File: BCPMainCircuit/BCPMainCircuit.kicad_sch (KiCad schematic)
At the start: 48 parts, among them Q1 IRLB8721PBF, SW1 Switch, U1 MCP9601T-E/MX, U2 Pico 2, U3 Logger, U4 GPS, U5 BNO055, U6 BME280, U7 MIC2940A-3.3WT, U8 MCP9601T-E/MX

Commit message: minor changes n stuff
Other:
- note added: "https://www.sparkfun.com/sparkfun-multiplexer-breakout-8-channel-74hc4051.html"
- moved on the sheet: C3, C4, R10, R11, R12, R13, R14, R15, R16, R17, R18, R5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

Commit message: e
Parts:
- added C10: 4u7F, Capacitor_SMD:C_0603_1608Metric, symbol Device:C_Small
- added C11, C5: 1uF, Capacitor_SMD:C_0603_1608Metric, symbol Device:C_Small
- added C6: 10uF, Capacitor_SMD:C_0805_2012Metric, symbol Device:C_Small
- added C7: 100nF, Capacitor_SMD:C_0603_1608Metric, symbol Device:C_Small
- added C8, C9: 22uF, Capacitor_SMD:C_0805_2012Metric, symbol Device:C_Small
- added J1: MSD-4-A, CUI_MSD-4-A:CUI_MSD-4-A, symbol Cosmos Schematic Symbols:MSD-4-A
- added L1: 4u7H, 74438357047:74438357047, symbol Device:L
- added RN1, RN2: CAY16-4702F4LF, CAY16-4702F4LF:RESCAF80P320X160X60-8N, symbol Cosmos Schematic Symbols:CAY16-4702F4LF
- added U9: AP63203WU-7, AP63203WU-7_DIO:AP63203WU-7_DIO, symbol Cosmos Schematic Symbols:AP63203WU-7
- R1: value ???R -> 20Ω
- R2, R3: value ???R -> 65Ω
- R4: value ???R -> 65v
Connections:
- net GND: now also C10.2, C11.2, C5.2, C6.2, C8.2, C9.2, J1.6 (VSS), J1.G1 (COVER_GND), J1.G2 (COVER_GND__1), J1.G3 (COVER_GND__2), J1.G4 (COVER_GND__3), U9.4 (GND)
- new net: C7.2, L1.2, U9.5 (SW)
- new net: C7.1, U9.6 (BST)
- new net: J1.1 (DAT2), RN2.8
- new net: J1.8 (DAT1), RN1.5
- new net +3V3: C10.1, C11.1, C5.1, C8.1, C9.1, J1.4 (VDD), L1.1, RN1.1, RN1.2, RN1.3, RN1.4, RN2.1, RN2.2, RN2.3, RN2.4, U9.1 (FB)
- new net BATT+: C6.1, U9.2 (EN), U9.3 (VIN)
- new net SD_CD: J1.CD, RN2.6
- new net SD_CS: J1.2 (CD/DAT3), RN2.7
- new net SD_MISO: J1.7 (DAT0), RN1.7
- new net SD_MOSI: J1.3 (CMD), RN1.6
- new net SD_SCK: J1.5 (CLK), RN1.8
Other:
- note added: "47k resistor network"
- note added: "Thermocouple Amplifier"
- note added: "Thermocouples + Multiplexers"
- note added: "microSD card connector"
- note added: "sd cd = card detect"
- note removed: "Thermals"
- moved on the sheet: C3, C4, R10, R11, R12, R13, R14, R15, R16, R17, R18, R5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

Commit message: e
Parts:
- R4: value 65v -> 65Ω
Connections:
- net +3.3V: now also C10.1, C11.1, C8.1, C9.1, L1.1, U9.1 (FB)
- net +3V3: no longer C10.1, C11.1, C8.1, C9.1, L1.1, U9.1 (FB)
- net BATT+: now also SW1.3 (A)
- net SD_CD: now also U2.27 (GPIO21)
- net SD_CS: now also U2.22 (GPIO17)
- net SD_MISO: now also U2.21 (GPIO16)
- net SD_MOSI: now also U2.25 (GPIO19)
- net SD_SCK: now also U2.24 (GPIO18)
- net TC-Sel1: now also U2.15 (GPIO11); no longer U2.27 (GPIO21)
- net TC-Sel2: now also U2.16 (GPIO12); no longer U2.26 (GPIO20)
- net TC-Sel3: now also U2.17 (GPIO13); no longer U2.25 (GPIO19)
- net ThermoOCwarn: now also U2.19 (GPIO14); no longer U2.22 (GPIO17)
- net ThermoSCwarn: now also U2.20 (GPIO15); no longer U2.21 (GPIO16)
- net at C1.1, U7.1 (IN): no longer SW1.3 (A)
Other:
- moved on the sheet: C1, C10, C11, C2, C5, C6, C7, C8, C9, J1, L1, R5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

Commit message: minor stuff working on SD card thing and tc amp and power Next steps: SMD components!!!
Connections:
- net +3.3V: now also J1.4 (VDD)
- net +3V3: no longer J1.4 (VDD)
- net VSense1: now also C3.1, R10.2, U1.2 (VIN+)
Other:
- note added: "TRASH?"
- moved on the sheet: C1, C2, C4, C5, J1, R12, R13, R14, R15, R16, R17, R18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

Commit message: lsm6dso
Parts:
- removed U5: BNO055, Trantor:BNO055, symbol Trantor:BNO055
- added C12, C13: 0u1f, symbol Device:C_Small
- added R19, R20: 10kΩ, Resistor_THT:R_Axial_DIN0207_L6.3mm_D2.5mm_P7.62mm_Horizontal, symbol Device:R_Small_US
- added U10: LSM6DSO, LGA-14L_2P5X3X0P86_STM, symbol LSM6DSO:LSM6DSO
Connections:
- net +3.3V: now also C12.1, C13.1, R19.1, R20.2, U10.5 (VDDIO), U10.8 (VDD)
- net GND: now also C12.2, C13.2, U10.2 (SDx), U10.3 (SCx), U10.6 (GND), U10.7 (GND)
- net SCL: now also R20.1, U10.13 (SCL)
- net SDA: now also R19.2, U10.14 (SDA)
- no-connect marks 30 -> 29
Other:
- note added: "ADDR:"
- note added: "SMD components make the jst connector 1x4 instead of 2 1x2s Breakout pins consider 16:2 SMD Mux"
- note removed: "ADDR: 29/28"
- note removed: "NOTES Flight LED moved to GPIO22 Debug LEDs moved to GPIO 7,8,9 IN REVERSE ORDER! ThermoSelect pins are 19,20,21 IN REVERSE ORDER! note: to use, just set the pins you need high, i can explain later"

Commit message: minor changes (everything is being redone using smd components instead of breakout boards) still need : gps antenna + schematic (capacitors?) IMU (current one needs 1.8v!!!!!!!!!!!!!!!!) RGB LEDs? 16:2 mux? sd card needs reviewing (why are things laid out that way???)
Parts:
- removed C1, C2: 10u, Capacitor_THT:C_Disc_D7.0mm_W2.5mm_P5.00mm, symbol Device:C
- removed C4: 0u1f, Capacitor_SMD:C_0201_0603Metric, symbol Device:C_Small
- removed R12, R16: 2M, Resistor_SMD:R_0201_0603Metric, symbol Device:R_US
- removed R13, R14: 100, Resistor_SMD:R_0201_0603Metric, symbol Device:R_US
- removed R15: 1M, Resistor_SMD:R_0201_0603Metric, symbol Device:R_US
- removed R17, R18: 10k, Resistor_SMD:R_0201_0603Metric, symbol Device:R_US
- removed U3: Logger, Trantor:MODULE_DEV-13712, symbol Trantor:DEV-13712
- removed U4: GPS, Gabriel_footprints:NEO-M9N GPS, symbol Trantor:GPS
- removed U6: BME280, Gabriel_footprints:BMP280, symbol Trantor:BME280
- removed U7: MIC2940A-3.3WT, Package_TO_SOT_THT:TO-220-3_Vertical, symbol Regulator_Linear:L7805
- removed U8: MCP9601T-E/MX, MQFN20_NU_MCH, symbol SMD_TC_AMP:MCP9601T-E_MX
- added C1: 200nf, Capacitor_SMD:C_0201_0603Metric, symbol Device:C_Small
- added R12, R13: 4.7kΩ, Resistor_SMD:R_0201_0603Metric, symbol Device:R_Small_US
- added U3: NEO-M9N-00B, Gabriel_footprints:NEO-M9N, symbol NEO-M9N:NEO-M9N-00B
- added U4: ICM-20948, Sensor_Motion:InvenSense_QFN-24_3x3mm_P0.4mm, symbol Sensor_Motion:ICM-20948
- added U5: BME280, Gabriel_footprints:BME280(1), symbol Sensor:BME280
- BT2: footprint Battery:BatteryHolder_Keystone_2462_2xAA -> Gabriel_footprints:BAT_1079
- C12, C13: footprint (none) -> Capacitor_SMD:C_0201_0603Metric
- J1: footprint CUI_MSD-4-A:CUI_MSD-4-A -> Gabriel_footprints:CUI_MSD-4-A
- L1: footprint 74438357047:74438357047 -> Inductor_SMD:L_0201_0603Metric
- R19, R20: footprint Resistor_THT:R_Axial_DIN0207_L6.3mm_D2.5mm_P7.62mm_Horizontal -> Resistor_SMD:R_0201_0603Metric
- RN1, RN2: footprint CAY16-4702F4LF:RESCAF80P320X160X60-8N -> Resistor_SMD:R_Array_Convex_4x1206
- TC2: footprint Connector_PinHeader_2.54mm:PinHeader_1x02_P2.54mm_Vertical -> (none)
- U1: footprint MQFN20_NU_MCH -> Gabriel_footprints:MQFN20_NU_MCH
- U10: footprint LGA-14L_2P5X3X0P86_STM -> (none)
- U9: footprint AP63203WU-7_DIO:AP63203WU-7_DIO -> Package_TO_SOT_SMD:TSOT-23-6
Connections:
- net +3V3 is gone; now on net +3.3V: C5.1, RN1.1, RN1.2, RN1.3, RN1.4, RN2.1, RN2.2, RN2.3, RN2.4
- net +3.3V: now also C1.1, R12.1, R13.2, U3.2 (D_SEL), U3.23 (VCC), U5.2 (CSB), U5.5 (SDO), U5.6 (VDDIO), U5.8 (VDD)
- net GND: now also C1.2, U3.10 (GND), U3.12 (GND), U3.13 (GND), U3.24 (GND), U5.1 (GND), U5.7 (GND)
- net SCL: now also R12.2, U3.19 (SCL_/_SPI_SLK), U5.4 (SCK)
- net SDA: now also R13.1, U3.18 (SDA_/_SPI_CS_N), U5.3 (SDI)
- net TimePulseGPS: now reaches U2.4 (GPIO2)
- net TimePulseGPS: now also U3.3 (TIMEPULSE)
- new net: U4.18 (GND), U4.20 (GND)
- new net +1.8V: U4.8 (VDDIO)
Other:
- note added: "Check Capacitor/Resistor sizes!!!!!!!!"
- note added: "gps antenna?????? Backup battery for faster start??? btw timepulse is a good error indicator capacitors????"
- note added: "https://www.sdcard.org/downloads/pls/pdf/?p=Part1_Physical_Layer_Simplified_Specification_Ver9.10.jpg&f=Part1PhysicalLayerSimplifiedSpecificationVer9.10Fin_20231201.pdf&e=EN_SS9_1"
- note added: "wtf is happening??"
- note removed: "60"
- note removed: "61"
- note removed: "62"
- note removed: "63"
- note removed: "64"
- note removed: "65"
- note removed: "66"
- note removed: "67"
- note removed: "TRASH?"
- moved on the sheet: C12, C13, R19, R20, U10

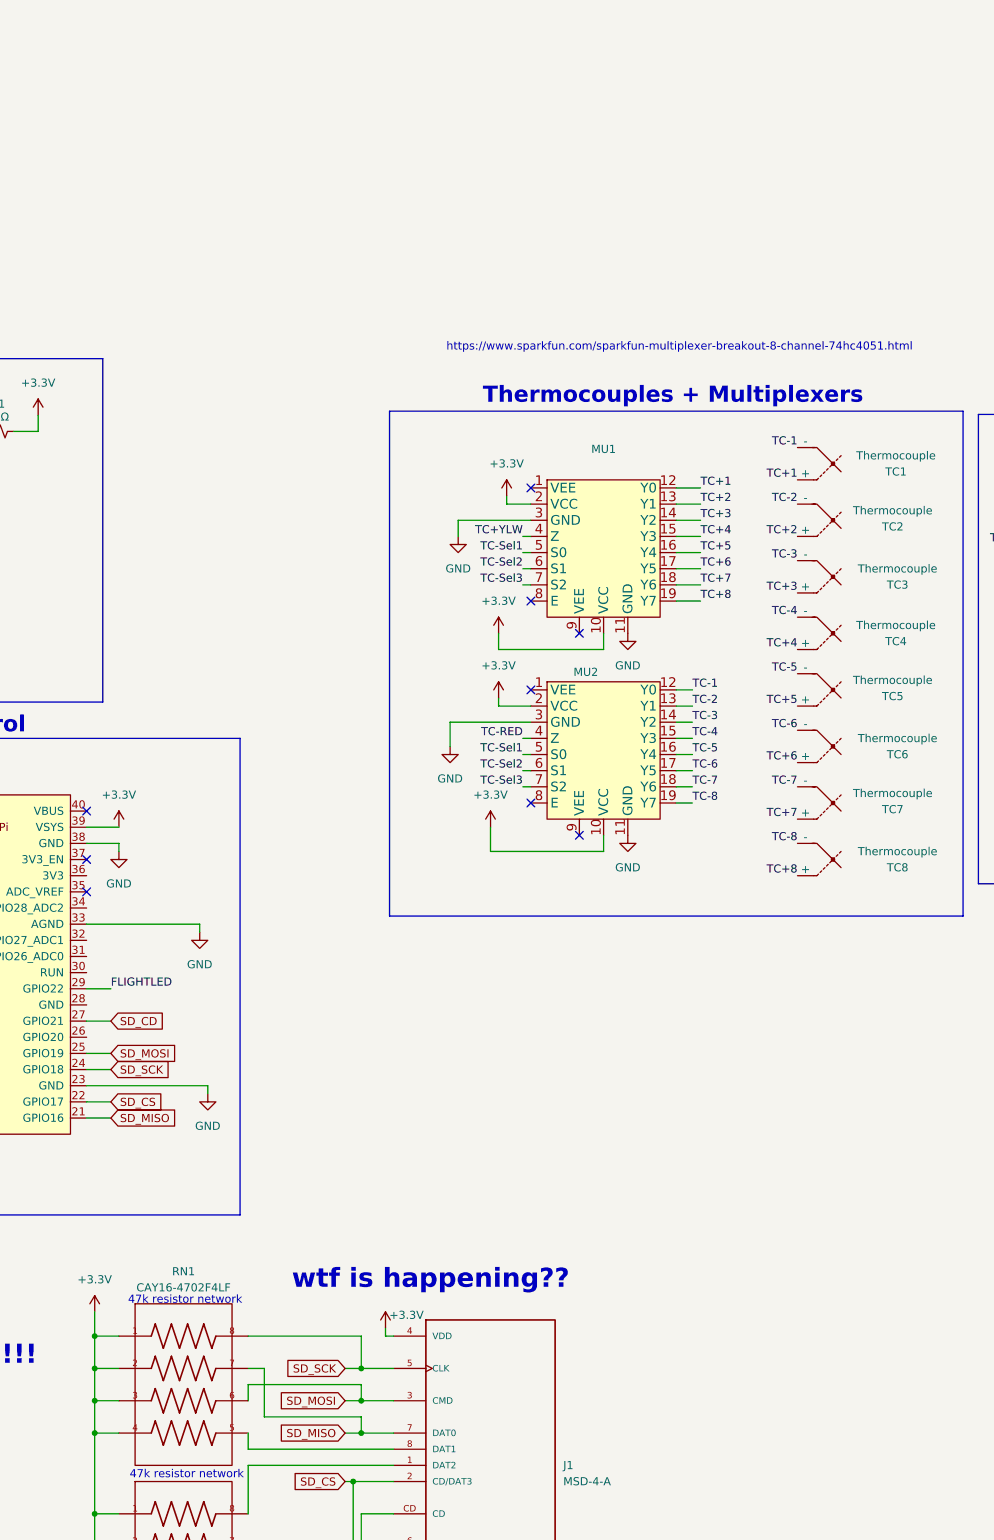
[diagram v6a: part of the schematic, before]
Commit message: in the middle of stuff NOTES: replace 2xmux with 1x cheaper mux? RGB leds HOW? how to sd card? magnetometer trade check stock of resistors, capacitors, inductors, sd slots, etc etc
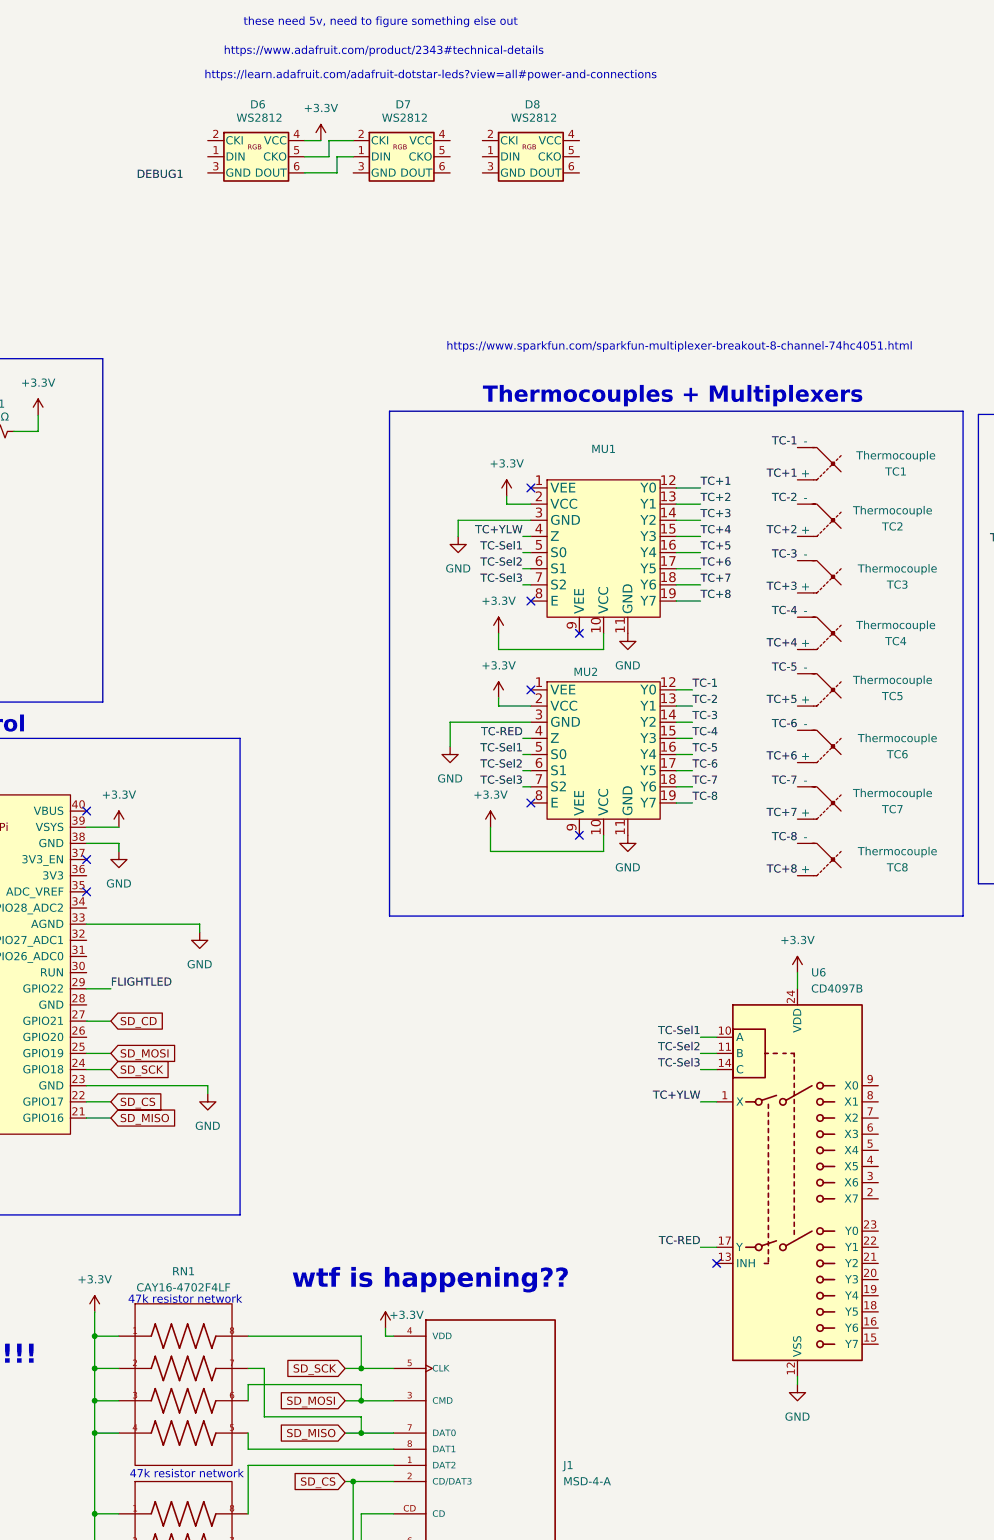
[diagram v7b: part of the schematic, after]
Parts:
- added D6, D7, D8: WS2812, LED_SMD:LED_WS2812_PLCC6_5.0x5.0mm_P1.6mm, symbol LED:WS2812
- added U6: CD4097B, symbol Analog_Switch:CD4097B
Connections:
- net +3.3V: now also D6.4 (VCC), U6.24 (VDD)
- net GND: now also U6.12 (VSS)
- net TC+YLW: now also U6.1 (X)
- net TC-RED: now also U6.17 (Y)
- net TC-Sel1: now also U6.10 (A)
- net TC-Sel2: now also U6.11 (B)
- net TC-Sel3: now also U6.14 (C)
- new net: D6.6 (DOUT), D7.1 (DIN)
- new net: D6.5 (CKO), D7.2 (CKI)
- no-connect marks 29 -> 30
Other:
- note added: "https://learn.adafruit.com/adafruit-dotstar-leds?view=all#power-and-connections"
- note added: "https://www.adafruit.com/product/2343#technical-details"
- note added: "these need 5v, need to figure something else out"

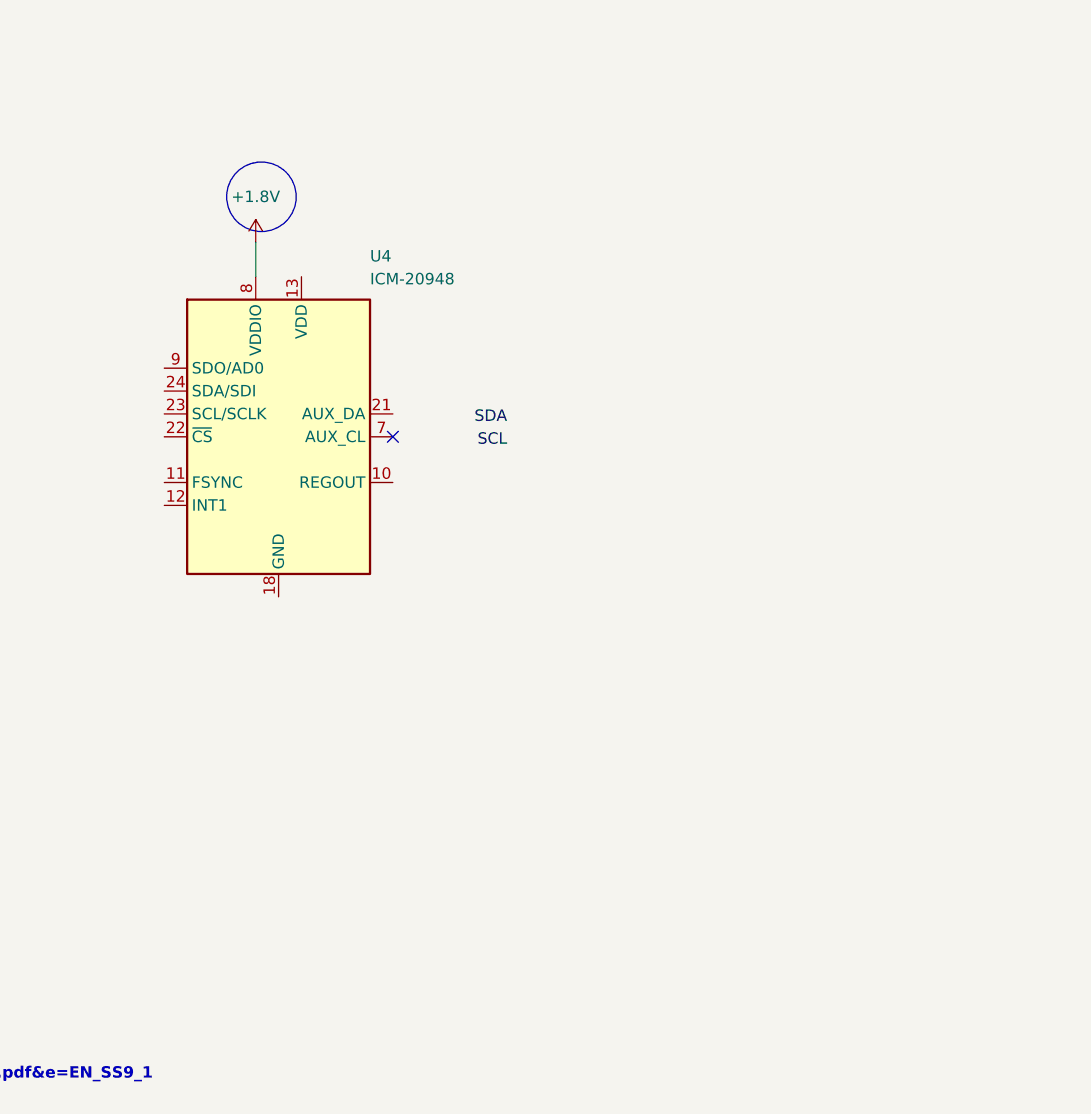
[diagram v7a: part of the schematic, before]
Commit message: finished magnetometer and imu still need: GPS stuff SD card stuff RGB LEDs
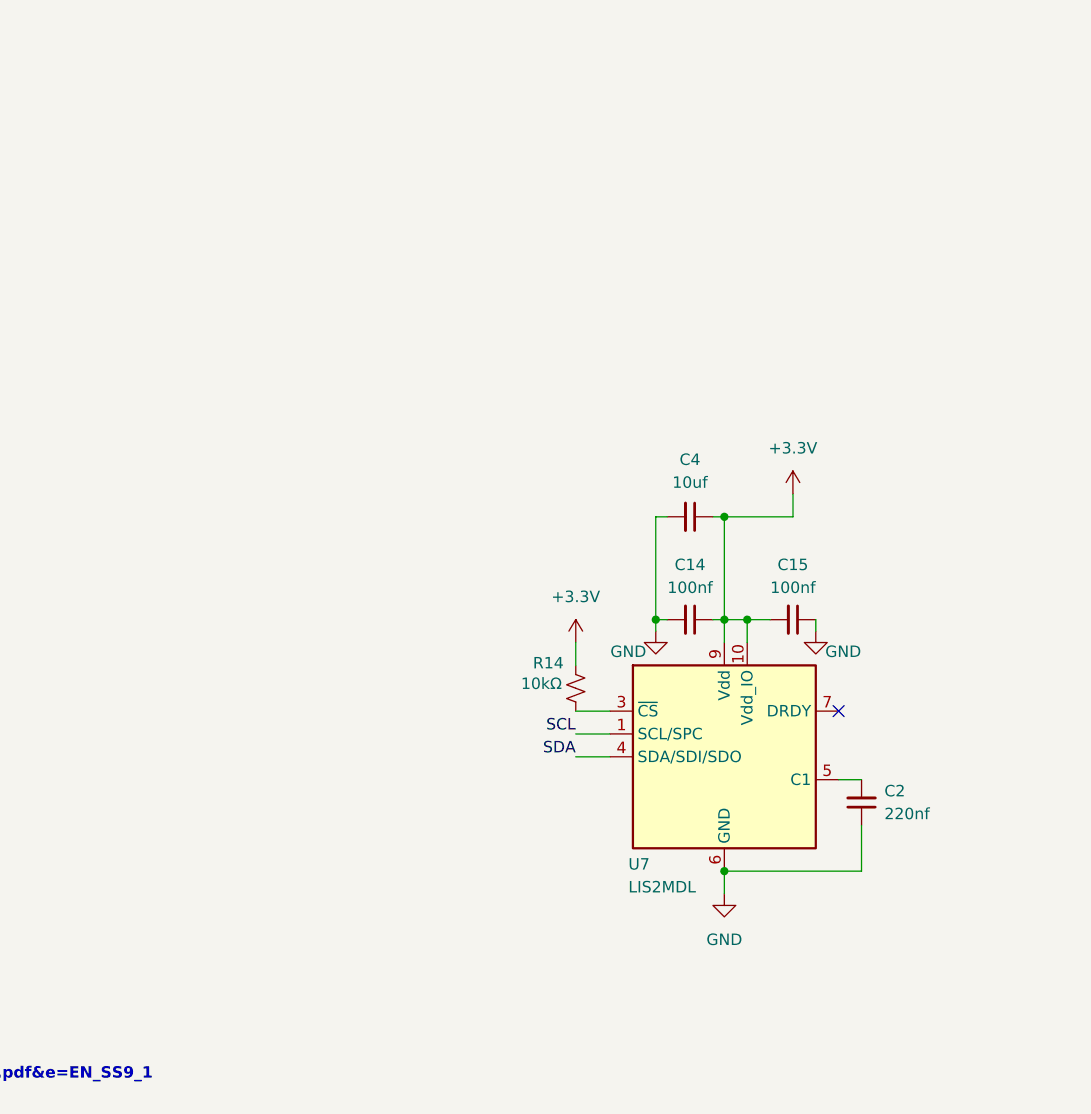
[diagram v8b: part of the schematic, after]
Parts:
- removed U4: ICM-20948, Sensor_Motion:InvenSense_QFN-24_3x3mm_P0.4mm, symbol Sensor_Motion:ICM-20948
- added C14, C15: 100nf, Capacitor_SMD:C_0201_0603Metric, symbol Device:C_Small
- added C2: 220nf, Capacitor_SMD:C_0201_0603Metric, symbol Device:C_Small
- added C4: 10uf, Capacitor_SMD:C_0201_0603Metric, symbol Device:C_Small
- added R14: 10kΩ, Resistor_SMD:R_0201_0603Metric, symbol Device:R_Small_US
- added U7: LIS2MDL, Package_LGA:LGA-12_2x2mm_P0.5mm, symbol Sensor_Magnetic:LIS2MDL
- U10: footprint (none) -> Gabriel_footprints:LSM6DSO
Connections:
- net +3.3V: now also C14.1, C15.2, C4.1, R14.1, U7.10 (Vdd_IO), U7.9 (Vdd)
- net GND: now also C14.2, C15.1, C2.1, C4.2, U7.6 (GND), U7.8 (GND)
- net SCL: now also U7.1 (SCL/SPC)
- net SDA: now also U7.4 (SDA/SDI/SDO)
- new net: R14.2, U7.3 (~{CS})
- new net: C2.2, U7.5 (C1)
